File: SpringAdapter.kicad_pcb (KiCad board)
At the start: 2 copper layers, 32 x 32.1 mm, 18 parts, among them J1 USB_C_Receptacle_USB2.0, J2 Conn_02x04_Odd_Even, SW1 SW_DIP_x01, U1 AP2112K-3.3

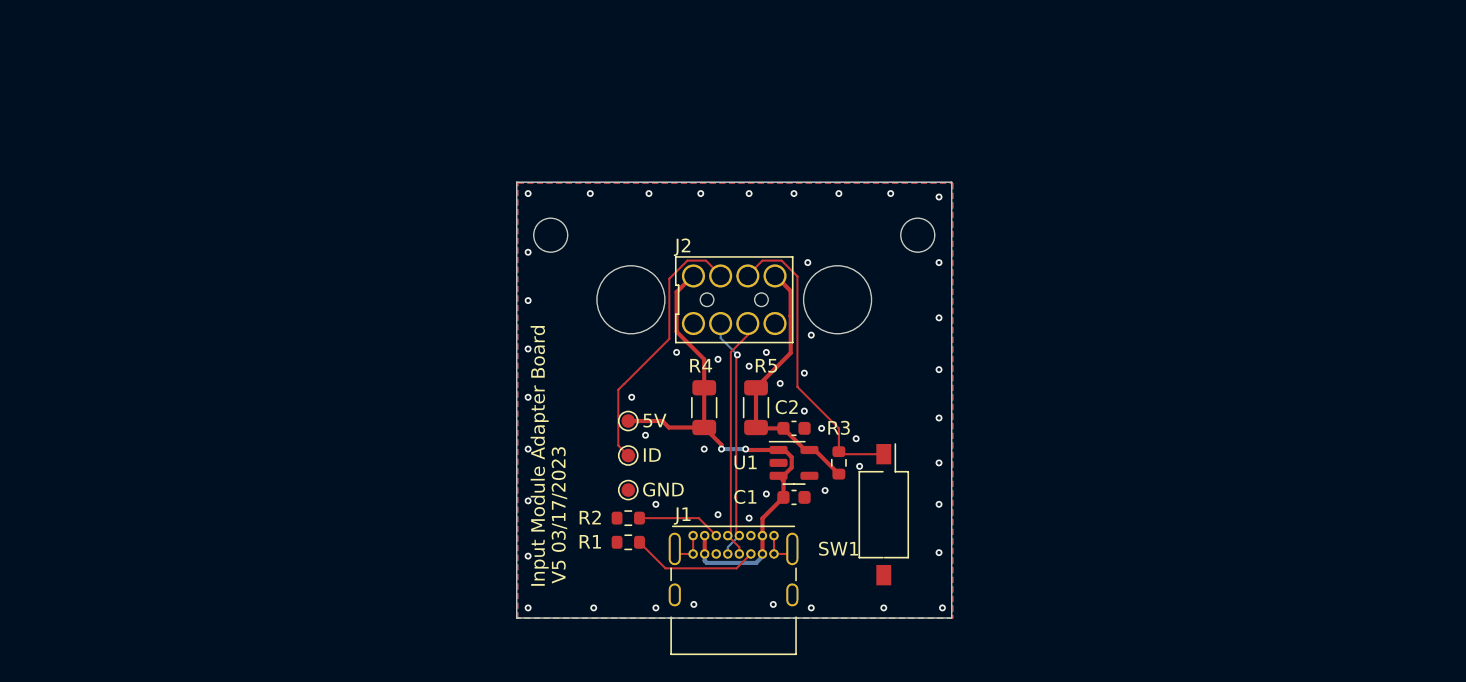
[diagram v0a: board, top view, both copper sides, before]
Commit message: Update repo to match JLCPCB parts, start adding USB hub
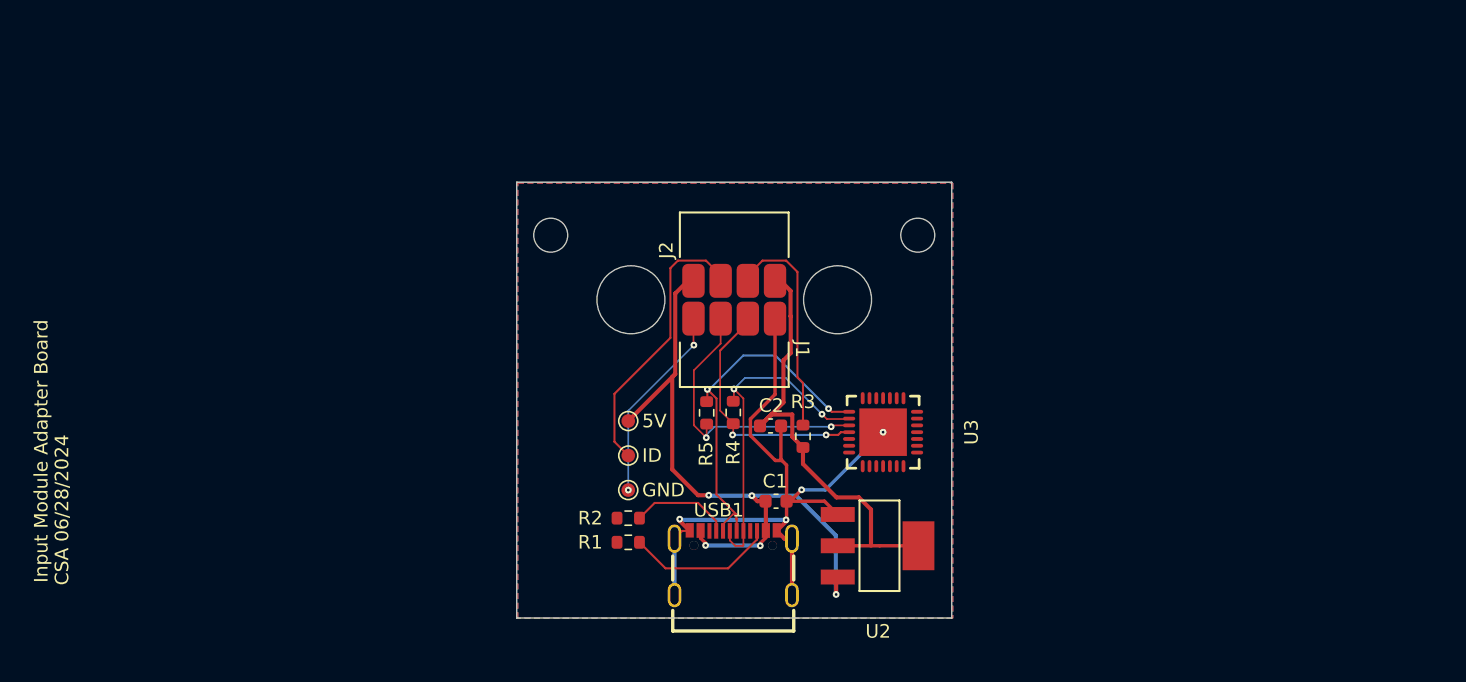
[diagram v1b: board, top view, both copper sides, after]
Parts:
- removed SW1: SW_DIP_x01, Button_Switch_SMD:SW_DIP_SPSTx01_Slide_Omron_A6S-110x_W8.9mm_P2.54mm
- removed U1: AP2112K-3.3, Package_TO_SOT_SMD:SOT-23-5
- added U2: AMS1117-3.3, ExternalMount:SOT-223-3_L6.5-W3.4-P2.30-LS7.0-BR, F.Cu at (126.6, 126.7)
- added U3: GL852G-OHY60_C7501404, ExternalMount:QFN-28_L5.0-W5.0-P0.50-BL-EP, F.Cu at (126.9, 118.4)
- added USB1: TYPE-C 16PIN 3MD(385), ExternalMount:USB-C-SMD_TYPE-C16PIN, F.Cu at (115.9, 128.0)
- J1: value USB_C_Receptacle_USB2.0 -> Molex 0472861001; footprint Connector_USB:USB_C_Receptacle_GCT_USB4085 -> ExternalMount:Molex_0472861001
- J2: value Conn_02x04_Odd_Even -> Molex 0472861001; footprint SpringAdapter:BP33242_2x4_P2.0mm -> ExternalMount:Molex_0472861001
- R4, R5: footprint Resistor_SMD:R_1206_3216Metric -> Resistor_SMD:R_0603_1608Metric
- moved J1 17.5 mm to (116.0, 108.8), turned to -90 degrees
- moved R5 3.65 mm to (114.0, 117.0), turned to -90 degrees
- moved R3 3.29 mm to (121.1, 118.7)
- moved R4 2.16 mm to (115.9, 116.9), turned to -90 degrees
- moved C2 1.74 mm to (118.7, 117.9)
- moved C1 1.35 mm to (119.1, 123.5)
- moved J2 0.14 mm to (116.0, 108.5), turned to 90 degrees
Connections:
- J2 pad 1: GND -> +3.3V
- J2 pad 2: +5V -> /~{SLEEP}
- J2 pad 3: /USB_D_N -> /BOARD_ID
- J2 pad 4: /BOARD_ID -> +5V
- R1 pad 1: Net-(J1-CC2) -> Net-(USB1-CC2)
- R2 pad 1: Net-(J1-CC1) -> Net-(USB1-CC1)
- R4 pad 1: +5V -> /USB_D_P
- R4 pad 2: +5V -> /USB_DP1
- R5 pad 1: +3.3V -> /USB_D_N
- R5 pad 2: +3.3V -> /USB_DM1
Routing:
- net GND: track 5.71 -> 68.6 mm, vias 51 -> 6
- net /USB_DM1: track 0.00 -> 22.0 mm, vias 0 -> 2
- net /USB_DP1: track 0.00 -> 18.2 mm, vias 0 -> 2
- net +3.3V: track 20.2 -> 34.2 mm
- net Net-(USB1-CC2): track 0.00 -> 11.0 mm
- net Net-(J1-CC2): track 9.43 -> 0.00 mm
- net /USB_D_N: track 18.0 -> 27.2 mm, vias 1 -> 2
- net +5V: track 40.9 -> 49.4 mm, vias 2 -> 5
- net Net-(USB1-CC1): track 0.00 -> 7.39 mm
- net /USB_D_P: track 18.0 -> 24.7 mm, vias 0 -> 2
- net /~{SLEEP}: track 22.1 -> 15.9 mm
- net Net-(J1-CC1): track 6.18 -> 0.00 mm
- net /BOARD_ID: track 19.6 -> 20.3 mm
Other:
- rule pad_to_mask_clearance: 0.0508 -> 0.04
- rule solder_mask_min_width: 0.101 -> 0.1
- board text added: "CSA 06/28/2024"
- board text removed: "V5 03/17/2023"

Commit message: First version complete
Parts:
- removed TP1: 5V, TestPoint:TestPoint_Pad_D1.0mm
- removed TP2: GND, TestPoint:TestPoint_Pad_D1.0mm
- removed TP3: BOARD_ID, TestPoint:TestPoint_Pad_D1.0mm
- removed U2: AMS1117-3.3, ExternalMount:SOT-223-3_L6.5-W3.4-P2.30-LS7.0-BR
- added C10: 22pF, Capacitor_SMD:C_0402_1005Metric, F.Cu at (89.1, 102.8)
- added C11: 22pF, Capacitor_SMD:C_0402_1005Metric, F.Cu at (95.0, 102.7)
- added C12: 100nF, Capacitor_SMD:C_0402_1005Metric, F.Cu at (86.9, 106.4)
- added C13: 10uF, Capacitor_SMD:C_0603_1608Metric, F.Cu at (109.9, 101.1)
- added C14: 100nF, Capacitor_SMD:C_0402_1005Metric, F.Cu at (110.5, 102.6)
- added C15: 10uF, Capacitor_SMD:C_0603_1608Metric, F.Cu at (122.0, 101.1)
- added C16: 100nF, Capacitor_SMD:C_0402_1005Metric, F.Cu at (121.4, 102.6)
- added C17: 10uF, Capacitor_SMD:C_0603_1608Metric, F.Cu at (143.9, 101.1)
- added C18: 100nF, Capacitor_SMD:C_0402_1005Metric, F.Cu at (144.5, 102.6)
- added C19: 10uF, Capacitor_SMD:C_0603_1608Metric, F.Cu at (156.0, 101.1)
- added C20: 100nF, Capacitor_SMD:C_0402_1005Metric, F.Cu at (155.4, 102.6)
- added C3: 100nF, Capacitor_SMD:C_0402_1005Metric, F.Cu at (96.2, 107.7)
- added C4: 100nF, Capacitor_SMD:C_0402_1005Metric, F.Cu at (94.5, 105.2)
- added C5: 100nF, Capacitor_SMD:C_0402_1005Metric, F.Cu at (88.7, 105.3)
- added C6: 10uF, Capacitor_SMD:C_0603_1608Metric, F.Cu at (86.2, 112.7)
- added C7: 100nF, Capacitor_SMD:C_0402_1005Metric, F.Cu at (86.9, 110.2)
- added C8: 10uF, Capacitor_SMD:C_0603_1608Metric, F.Cu at (96.6, 113.7)
- added C9: 100nF, Capacitor_SMD:C_0402_1005Metric, F.Cu at (93.1, 113.2)
- added H5: MountingHole, MountingHole:MountingHole_5mm, F.Cu at (157.6, 108.7)
- added H6: MountingHole, MountingHole:MountingHole_5mm, F.Cu at (142.4, 108.7)
- added H7: MountingHole, MountingHole:MountingHole_2.5mm, F.Cu at (136.5, 103.9)
- added H8: MountingHole, MountingHole:MountingHole_2.5mm, F.Cu at (163.5, 103.9)
- added J3: Molex 0472861001, ExternalMount:Molex_0472861001, F.Cu at (150.0, 108.8)
- added J4: Molex 0472861001, ExternalMount:Molex_0472861001, F.Cu at (150.0, 108.5)
- added L1: 10u, Inductor_SMD:L_0805_2012Metric, F.Cu at (96.7, 111.9)
- added R10: 20k, Resistor_SMD:R_0402_1005Metric, F.Cu at (90.9, 113.2)
- added R11: 100k, Resistor_SMD:R_0402_1005Metric, F.Cu at (88.7, 113.2)
- added R12: 0, Resistor_SMD:R_0402_1005Metric, F.Cu at (89.8, 113.2)
- added R13: 10k, Resistor_SMD:R_0402_1005Metric, F.Cu at (87.6, 113.2)
- added R6: 680 1%, Resistor_SMD:R_0603_1608Metric, F.Cu at (97.1, 106.0)
- added R7: 47k, Resistor_SMD:R_0402_1005Metric, F.Cu at (86.9, 107.6)
- added R8: 10k, Resistor_SMD:R_0402_1005Metric, F.Cu at (86.9, 108.9)
- added R9: 10k, Resistor_SMD:R_0402_1005Metric, F.Cu at (92.0, 113.2)
- added U1: XC6206P332MR-G, Package_TO_SOT_SMD:SOT-23-3, F.Cu at (95.9, 95.9)
- added X1: 12MHz, ExternalMount:OSC-SMD_4P-L3.2-W2.5-BL, F.Cu at (92.1, 102.8)
- R1, R2, R3, R4, R5: footprint Resistor_SMD:R_0603_1608Metric -> Resistor_SMD:R_0402_1005Metric
- moved USB1 42.5 mm to (89.2, 95.0), turned to -90 degrees
- moved U3 36.7 mm to (91.6, 108.7), turned to 90 degrees
- moved C1 33.4 mm to (96.5, 98.9)
- moved C2 33.4 mm to (96.5, 93.0), turned to 180 degrees
- moved R1 31.7 mm to (87.2, 102.8), turned to -90 degrees
- moved R2 31.3 mm to (85.9, 102.8), turned to -90 degrees
- moved R3 27.4 mm to (94.2, 113.2), turned to -90 degrees
- moved R4 21.3 mm to (96.2, 109.0), turned to 0 degrees
- moved R5 19.0 mm to (96.2, 110.3), turned to 0 degrees
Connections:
- C2 pad 1: +3.3V -> +3.3VP
- J2 pad 1: +3.3V -> +3.3VP
- J2 pad 3: /BOARD_ID -> unconnected-(J2-Pin_3-Pad3)
- U3 pad 10: unconnected-(U3-X1-Pad10) -> Net-(U3-X1)
- U3 pad 11: unconnected-(U3-X2-Pad11) -> Net-(U3-X2)
- U3 pad 14: unconnected-(U3-AVDD-Pad14) -> /AVDD
- U3 pad 17: unconnected-(U3-~{RESET}-Pad17) -> /RESET
- U3 pad 18: unconnected-(U3-TEST/SCL-Pad18) -> GND
- U3 pad 21: unconnected-(U3-DVDD-Pad21) -> +3.3V
- U3 pad 22: unconnected-(U3-PSELF-Pad22) -> Net-(U3-PSELF)
- U3 pad 23: unconnected-(U3-PGANG-Pad23) -> Net-(U3-PGANG)
- U3 pad 25: unconnected-(U3-~{OVCUR1}-Pad25) -> /OVCURR
- U3 pad 27: unconnected-(U3-V5-Pad27) -> +5V
- U3 pad 28: unconnected-(U3-V33-Pad28) -> +3.3V
- U3 pad 5: unconnected-(U3-AVDD-Pad5) -> /AVDD
- U3 pad 8: unconnected-(U3-RREF-Pad8) -> /RREF
- U3 pad 9: unconnected-(U3-AVDD-Pad9) -> /AVDD
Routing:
- net GND: track 68.6 -> 257.8 mm, vias 6 -> 28
- net +3.3VP: track 0.00 -> 81.7 mm, vias 0 -> 3
- net /~{SLEEP}: track 15.9 -> 91.6 mm, vias 0 -> 4
- net /USB_DM2: track 0.00 -> 63.9 mm, vias 0 -> 2
- net /USB_DP2: track 0.00 -> 63.8 mm, vias 0 -> 2
- net +5V: track 49.4 -> 112.3 mm, vias 5 -> 6
- net /BOARD_ID: track 20.3 -> 0.00 mm
- net /AVDD: track 0.00 -> 19.2 mm, vias 0 -> 5
- net +3.3V: track 34.2 -> 17.9 mm, vias 0 -> 2
- net /USB_DP1: track 18.2 -> 32.0 mm
- net /USB_D_P: track 24.7 -> 36.1 mm, vias 2 -> 3
- net /USB_DM1: track 22.0 -> 31.9 mm
- net /USB_D_N: track 27.2 -> 34.9 mm
- net Net-(U3-X1): track 0.00 -> 6.66 mm
- net Net-(U3-X2): track 0.00 -> 4.83 mm
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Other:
- board size 32 x 32.1 mm -> 81.7 x 26.6 mm
- board text removed: "5V"
- board text removed: "GND"
- board text removed: "ID"
